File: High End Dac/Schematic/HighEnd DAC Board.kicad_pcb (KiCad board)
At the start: 2 copper layers, 26 parts, among them CON1 CONN_01X13, P1 10K, P2 10K, U1 LT1012, U2 LT1012, U3 LTC2756, U4 LTC6655, U5 LM7805

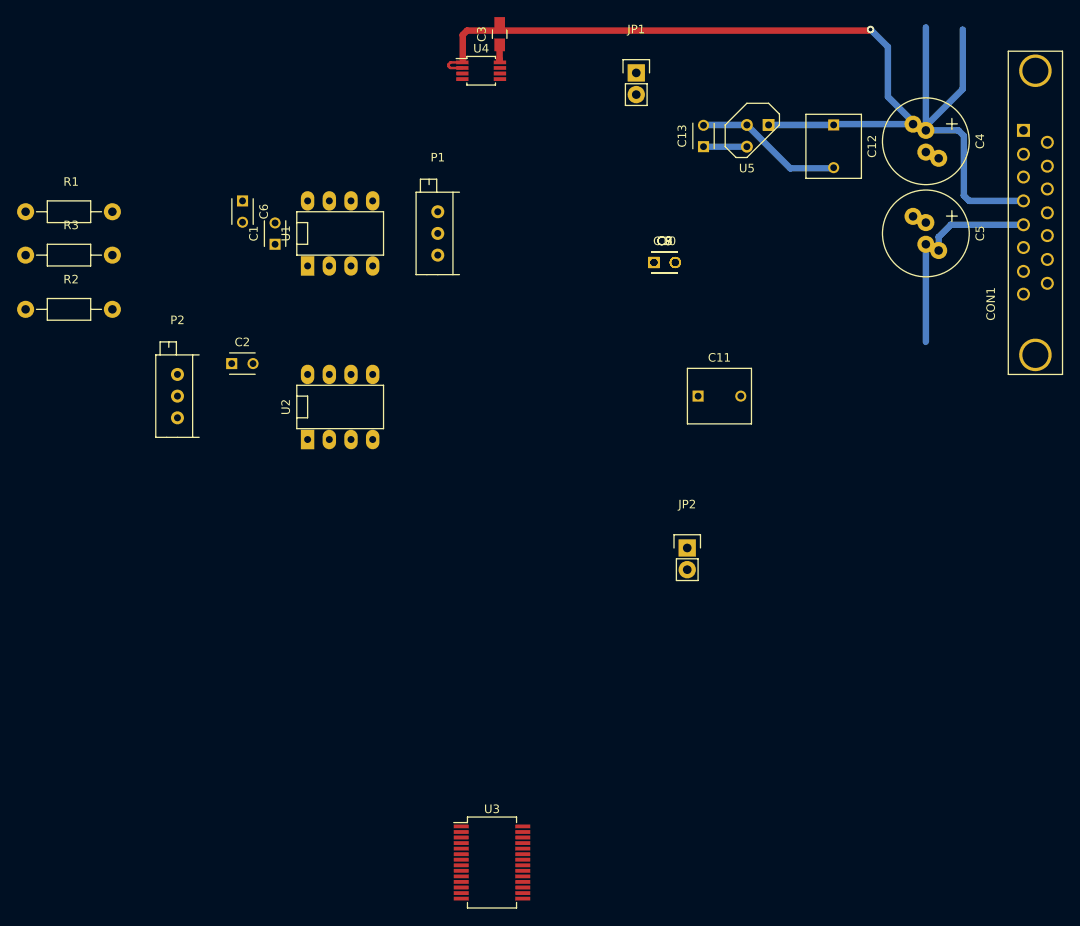
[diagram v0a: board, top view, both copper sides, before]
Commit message: Added some PI Filter to the supply rails
Added some PI Filter to the supply rails
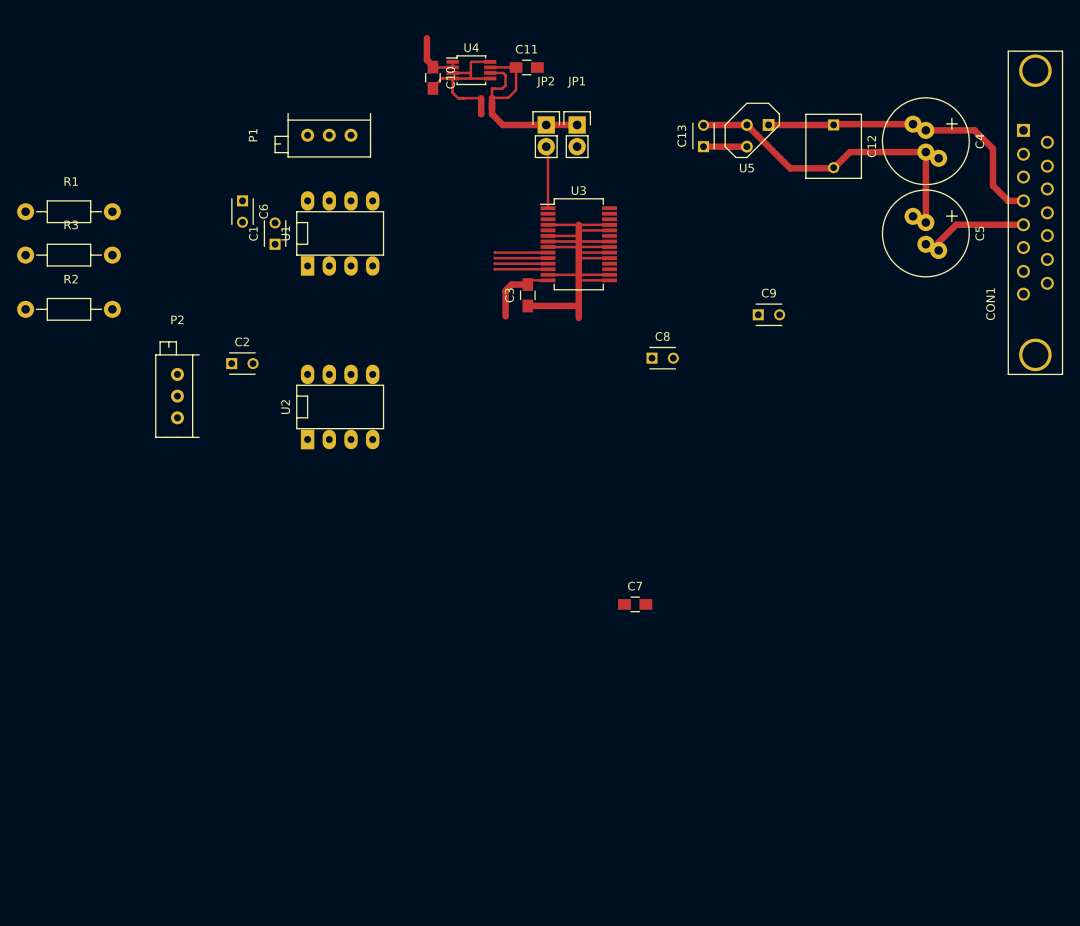
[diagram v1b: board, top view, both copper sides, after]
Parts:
- C10, C7: footprint Capacitors_ThroughHole:C_Disc_D3_P2.5 -> Capacitors_SMD:C_0805_HandSoldering
- C11: footprint Capacitors_ThroughHole:C_Rect_L7.5_W6.5_P5 -> Capacitors_SMD:C_0805_HandSoldering
- moved U3 73.1 mm to (139.7, 102.9)
- moved JP2 52.2 mm to (135.9, 88.9)
- moved C11 43.4 mm to (133.6, 82.2)
- moved C7 40.1 mm to (146.3, 145.0)
- moved C10 33.7 mm to (122.6, 83.4), turned to 270 degrees
- moved C3 30.7 mm to (133.7, 108.8)
- moved P1 17.3 mm to (113.0, 90.1), turned to 90 degrees
- moved C9 13.7 mm to (160.7, 111.1)
- moved C8 11.2 mm to (148.3, 116.2)
- moved JP1 9.22 mm to (139.5, 88.9)
- moved U4 1.14 mm to (127.1, 82.5)
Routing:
- net GND: track 18.6 -> 129.3 mm
- net +15V: track 129.3 -> 41.6 mm, vias 1 -> 0
- net Net-(C11-Pad1): track 0.00 -> 27.4 mm
- net -15V: track 23.5 -> 11.7 mm
- net +5V: track 5.08 -> 13.6 mm
- net /REF: track 0.00 -> 7.29 mm
- net /SDI: track 0.00 -> 6.26 mm
- net /~CS~/LD: track 0.00 -> 6.25 mm
- net /SCK: track 0.00 -> 6.25 mm
- net /SRO: track 0.00 -> 6.24 mm
